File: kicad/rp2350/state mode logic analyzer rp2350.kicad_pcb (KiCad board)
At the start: 4 copper layers, 65.9 x 81.5 mm, 95 parts, among them J1 USB0, J10 Vcca_select, J2 JST_SH_BM04B-SRSS-TB, J3 Probe_Hi, J4 Probe Power, J5 Probe_Lo, J6 Probe Power, J7 SWD0, J8 FTDI Header, J9 Vccb_select, U1 MCP4725A2T-E/CH, U12 SN74LVC8T245DBQR, U13 SN74LVC2T45DCTRE4, U2 RP2350_Stamp_XL, U4 SN74LVC8T245DBQR, U5 SN74LVC8T245DBQR, U6 SN74LVC8T245DBQR

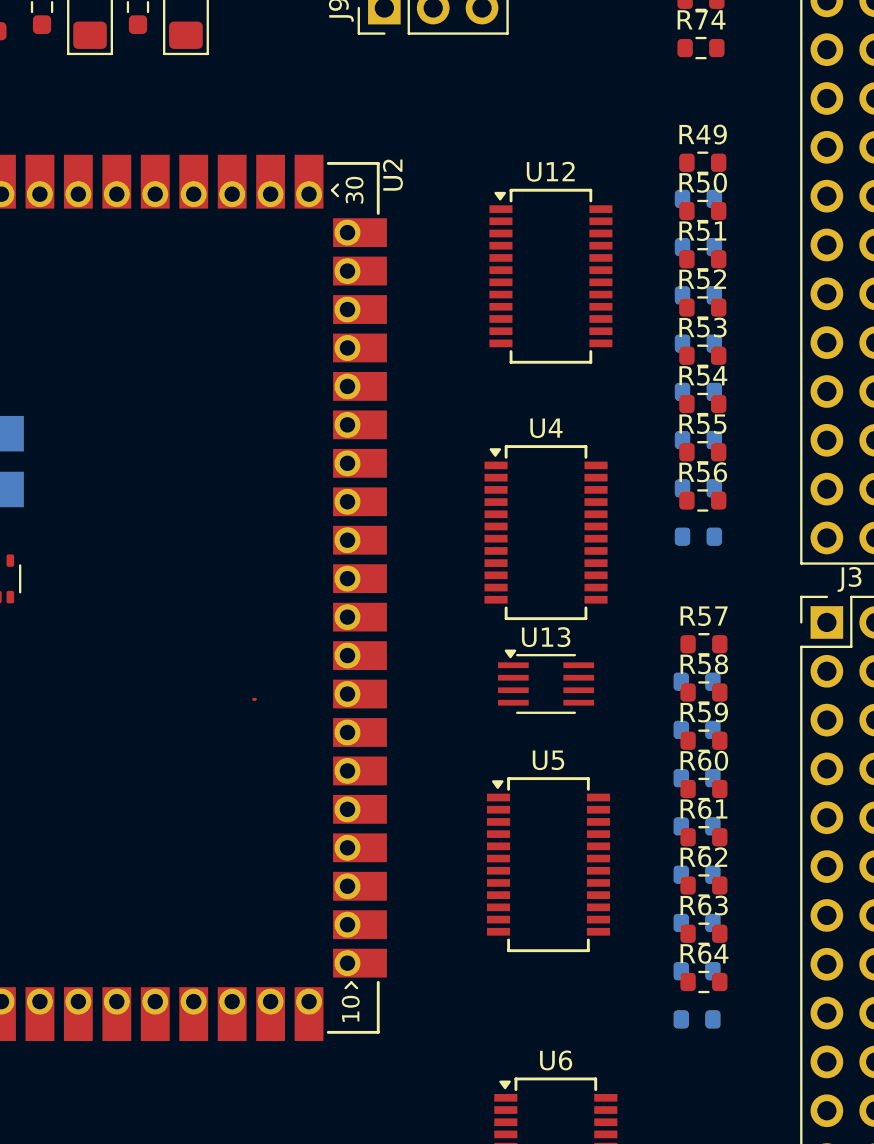
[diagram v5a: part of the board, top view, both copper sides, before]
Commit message: replaces term resistors with arrays
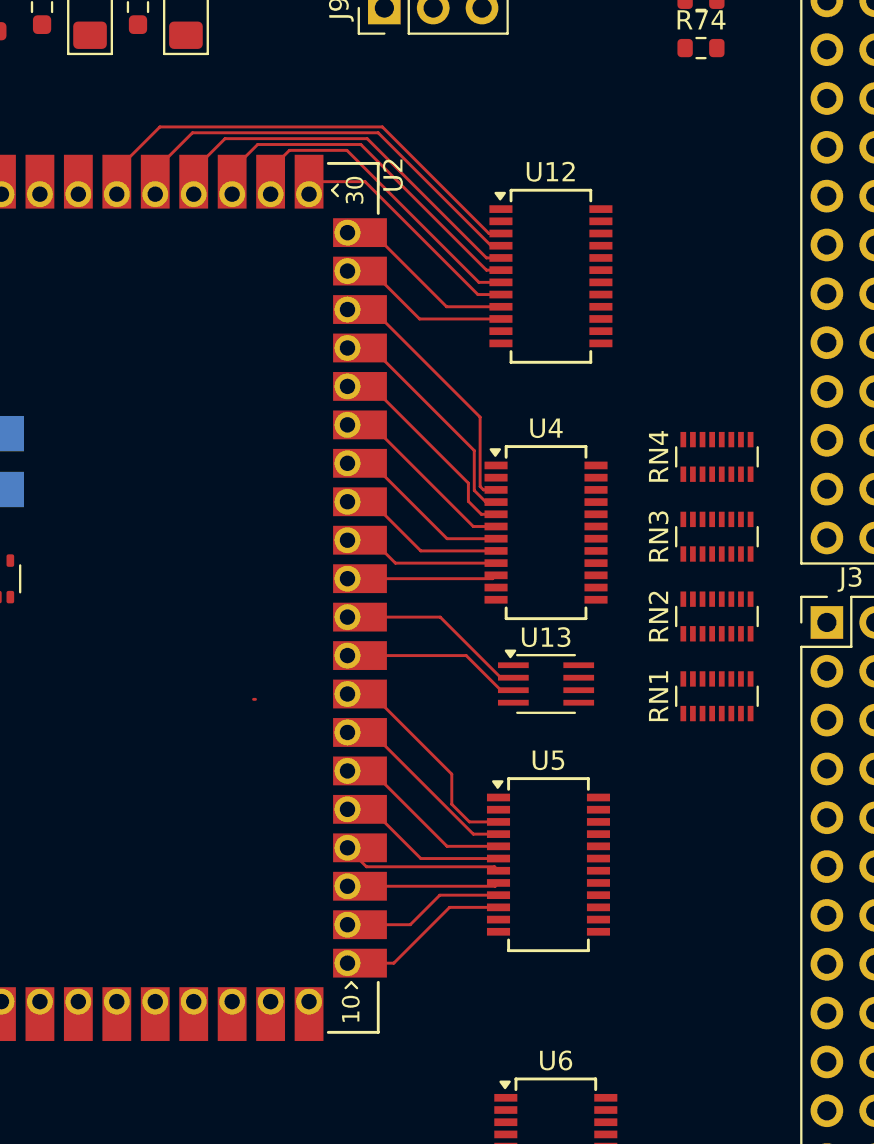
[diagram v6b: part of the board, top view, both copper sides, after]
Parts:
- removed R25, R26, R27, R28, R29, R30, R31, R32, R33, R34, R35, R36, R37, R38, R39, R40, R49, R50, R51, R52, R53, R54, R55, R56, R57, R58, R59, R60, R61, R62, R63, R64: 220, Resistor_SMD:R_0603_1608Metric
- added RN1: YC248-FR-07220RL, Resistor_SMD:R_Array_Convex_8x0602, F.Cu at (125.5, 63.9)
- added RN2: YC248-FR-07220RL, Resistor_SMD:R_Array_Convex_8x0602, F.Cu at (125.5, 59.7)
- added RN3: YC248-FR-07220RL, Resistor_SMD:R_Array_Convex_8x0602, F.Cu at (125.5, 55.6)
- added RN4: YC248-FR-07220RL, Resistor_SMD:R_Array_Convex_8x0602, F.Cu at (125.5, 51.4)
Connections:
- R73 pad 2: /INQUAL -> /INCLK
- R74 pad 2: /INCLK -> /INQUAL
- U12 pad 14: /B0 -> /B7
- U12 pad 15: /B1 -> /B6
- U12 pad 16: /B2 -> /B5
- U12 pad 17: /B3 -> /B4
- U12 pad 18: /B4 -> /B3
- U12 pad 19: /B5 -> /B2
- U12 pad 20: /B6 -> /B1
- U12 pad 21: /B7 -> /B0
- U13 pad 2: /QUAL -> /CLK
- U13 pad 3: /CLK -> /QUAL
- U4 pad 14: /B8 -> /B15
- U4 pad 15: /B9 -> /B14
- U4 pad 16: /B10 -> /B13
- U4 pad 17: /B11 -> /B12
- U4 pad 18: /B12 -> /B11
- U4 pad 19: /B13 -> /B10
- U4 pad 20: /B14 -> /B9
- U4 pad 21: /B15 -> /B8
- U5 pad 14: /B16 -> /B23
- U5 pad 15: /B17 -> /B22
- U5 pad 16: /B18 -> /B21
- U5 pad 17: /B19 -> /B20
- U5 pad 18: /B20 -> /B19
- U5 pad 19: /B21 -> /B18
- U5 pad 20: /B22 -> /B17
- U5 pad 21: /B23 -> /B16
- U6 pad 14: /B24 -> /B31
- U6 pad 15: /B25 -> /B30
- U6 pad 16: /B26 -> /B29
- U6 pad 17: /B27 -> /B28
- U6 pad 18: /B28 -> /B27
- U6 pad 19: /B29 -> /B26
- U6 pad 20: /B30 -> /B25
- U6 pad 21: /B31 -> /B24
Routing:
- net /BUF00: track 0.00 -> 23.8 mm
- net /BUF01: track 0.00 -> 22.5 mm
- net /BUF02: track 0.00 -> 20.5 mm
- net /BUF03: track 0.00 -> 18.5 mm
- net /BUF04: track 0.00 -> 15.9 mm
- net /BUF08: track 0.00 -> 13.1 mm
- net /BUF05: track 0.00 -> 12.4 mm
- net /BUF09: track 0.00 -> 12.3 mm
- net /BUF16: track 0.00 -> 11.5 mm
- net /BUF10: track 0.00 -> 10.4 mm
- net /BUF17: track 0.00 -> 10.0 mm
- net /QUAL: track 0.00 -> 10.0 mm
- net /CLK: track 0.00 -> 9.93 mm
- net /BUF11: track 0.00 -> 9.92 mm
- net /BUF12: track 0.00 -> 9.35 mm
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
